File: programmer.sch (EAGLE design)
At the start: 2 parts, among them U1 ATMEGA328P_PDIP

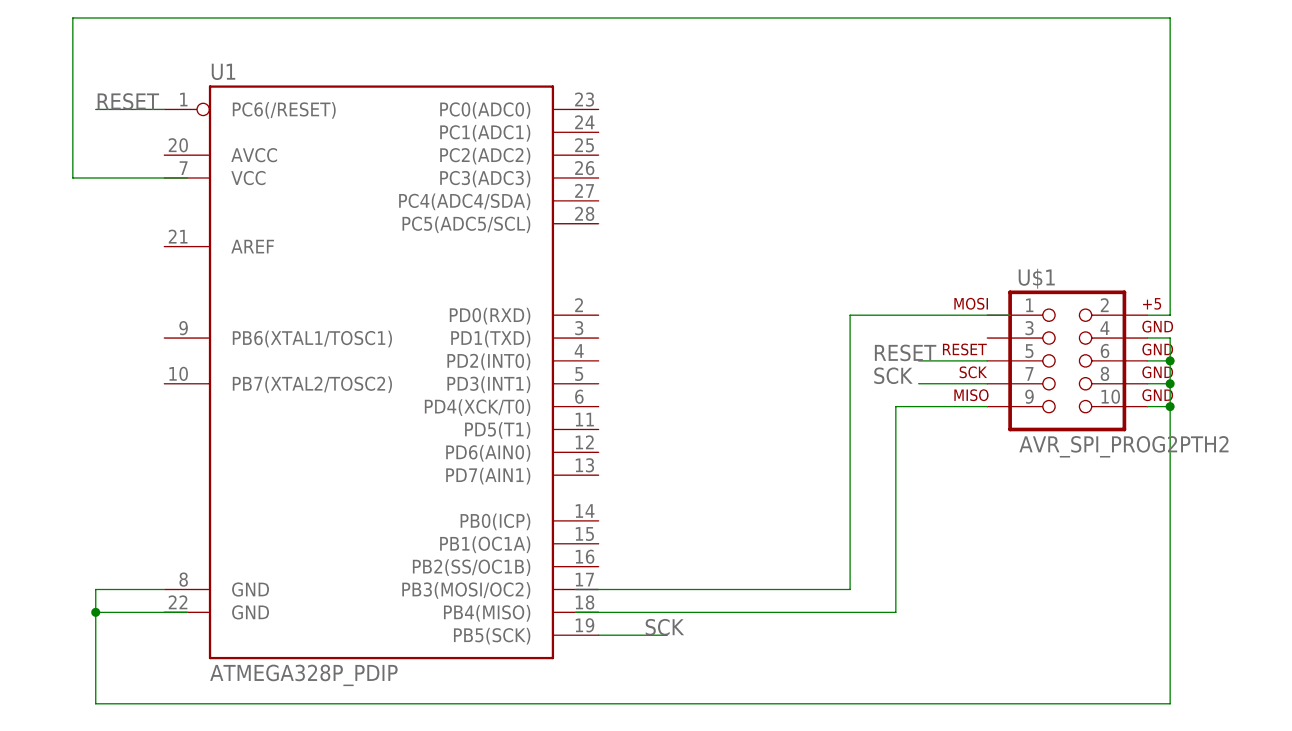
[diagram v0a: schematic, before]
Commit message: Added header for crystal and caps, cleaned VCC and GND lines
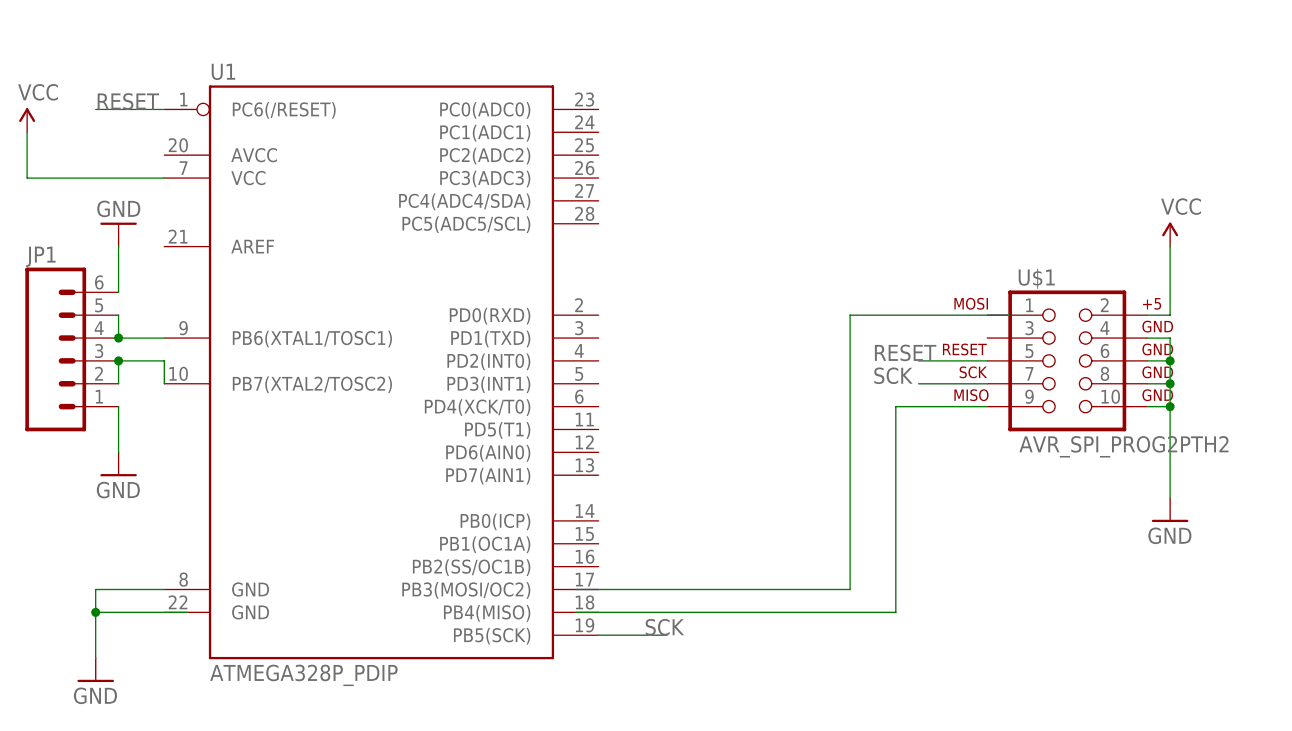
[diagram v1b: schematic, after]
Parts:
- added JP1: (no value), SparkFun-Connectors:M06LOCK
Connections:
- removed net N$4: U$1.10, U$1.4, U$1.6, U$1.8, U1.GND@1
- new net GND: JP1.1, JP1.6, U$1.10, U$1.4, U$1.6, U$1.8, U1.GND@1
- new net N$3: JP1.4, JP1.5, U1.PB6(XTAL1/TOSC1)
- new net N$5: JP1.2, JP1.3, U1.PB7(XTAL2/TOSC2)
- net VCC: now also U1.VCC
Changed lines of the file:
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@@
 <part name="U1" library="SparkFun-DigitalIC" deviceset="ATMEGA328P_PDIP" device=""/>
 <part name="U$1" library="SparkFun-Connectors" deviceset="AVR_SPI_PROG2" device="PTH2"/>
+<part name="JP1" library="SparkFun-Connectors" deviceset="M06" device="LOCK"/>
+<part name="GND1" library="SparkFun-Aesthetics" deviceset="GND" device=""/>
+<part name="GND2" library="SparkFun-Aesthetics" deviceset="GND" device=""/>
+<part name="GND3" library="SparkFun-Aesthetics" deviceset="GND" device=""/>
+<part name="GND4" library="SparkFun-Aesthetics" deviceset="GND" device=""/>
+<part name="SUPPLY1" library="SparkFun-Aesthetics" deviceset="VCC" device=""/>
+<part name="SUPPLY2" library="SparkFun-Aesthetics" deviceset="VCC" device=""/>
 </parts>
 <sheets>
@@
 <instance part="U1" gate="G$1" x="30.48" y="63.5"/>
 <instance part="U$1" gate="A" x="106.68" y="60.96"/>
+<instance part="JP1" gate="G$1" x="-2.54" y="60.96"/>
+<instance part="GND1" gate="1" x="119.38" y="43.18"/>
+<instance part="GND2" gate="1" x="0" y="25.4"/>
+<instance part="GND3" gate="1" x="2.54" y="48.26"/>
+<instance part="GND4" gate="1" x="2.54" y="76.2" rot="R180"/>
+<instance part="SUPPLY1" gate="G$1" x="119.38" y="73.66"/>
+<instance part="SUPPLY2" gate="G$1" x="-7.62" y="86.36"/>
 </instances>
 <busses>
@@
 </segment>
 </net>
-<net name="N$4" class="0">
+<net name="VCC" class="0">
 <segment>
+<pinref part="U$1" gate="A" pin="2"/>
+<wire x1="116.84" y1="66.04" x2="119.38" y2="66.04" width="0.1524" layer="91"/>
+<pinref part="SUPPLY1" gate="G$1" pin="VCC"/>
+<wire x1="119.38" y1="66.04" x2="119.38" y2="73.66" width="0.1524" layer="91"/>
+</segment>
+<segment>
+<pinref part="U1" gate="G$1" pin="VCC"/>
+<pinref part="SUPPLY2" gate="G$1" pin="VCC"/>
+<wire x1="7.62" y1="81.28" x2="-7.62" y2="81.28" width="0.1524" layer="91"/>
+<wire x1="-7.62" y1="81.28" x2="-7.62" y2="86.36" width="0.1524" layer="91"/>
+</segment>
+</net>
+<net name="N$3" class="0">
+<segment>
+<pinref part="U1" gate="G$1" pin="PB6(XTAL1/TOSC1)"/>
+<pinref part="JP1" gate="G$1" pin="4"/>
+<wire x1="7.62" y1="63.5" x2="2.54" y2="63.5" width="0.1524" layer="91"/>
+<pinref part="JP1" gate="G$1" pin="5"/>
+<wire x1="2.54" y1="63.5" x2="2.54" y2="66.04" width="0.1524" layer="91"/>
+<junction x="2.54" y="63.5"/>
+</segment>
+</net>
+<net name="N$5" class="0">
+<segment>
+<pinref part="JP1" gate="G$1" pin="3"/>
+<pinref part="U1" gate="G$1" pin="PB7(XTAL2/TOSC2)"/>
+<wire x1="2.54" y1="60.96" x2="7.62" y2="60.96" width="0.1524" layer="91"/>
+<wire x1="7.62" y1="60.96" x2="7.62" y2="58.42" width="0.1524" layer="91"/>
+<pinref part="JP1" gate="G$1" pin="2"/>
+<wire x1="2.54" y1="60.96" x2="2.54" y2="58.42" width="0.1524" layer="91"/>
+<junction x="2.54" y="60.96"/>
+</segment>
+</net>
+<net name="GND" class="0">
+<segment>
+<pinref part="U$1" gate="A" pin="8"/>
+<wire x1="116.84" y1="58.42" x2="119.38" y2="58.42" width="0.1524" layer="91"/>
+<pinref part="U$1" gate="A" pin="6"/>
+<wire x1="116.84" y1="60.96" x2="119.38" y2="60.96" width="0.1524" layer="91"/>
+<pinref part="U$1" gate="A" pin="4"/>
+<wire x1="116.84" y1="63.5" x2="119.38" y2="63.5" width="0.1524" layer="91"/>
+<wire x1="119.38" y1="63.5" x2="119.38" y2="60.96" width="0.1524" layer="91"/>
+<junction x="119.38" y="60.96"/>
+<wire x1="119.38" y1="60.96" x2="119.38" y2="58.42" width="0.1524" layer="91"/>
+<junction x="119.38" y="58.42"/>
+<wire x1="119.38" y1="58.42" x2="119.38" y2="55.88" width="0.1524" layer="91"/>
 <pinref part="U$1" gate="A" pin="10"/>
 <wire x1="116.84" y1="55.88" x2="119.38" y2="55.88" width="0.1524" layer="91"/>
-<wire x1="119.38" y1="55.88" x2="119.38" y2="22.86" width="0.1524" layer="91"/>
-<wire x1="119.38" y1="22.86" x2="0" y2="22.86" width="0.1524" layer="91"/>
-<wire x1="0" y1="22.86" x2="0" y2="33.02" width="0.1524" layer="91"/>
+<pinref part="GND1" gate="1" pin="GND"/>
+<wire x1="119.38" y1="55.88" x2="119.38" y2="45.72" width="0.1524" layer="91"/>
+<junction x="119.38" y="55.88"/>
+</segment>
+<segment>
 <wire x1="0" y1="33.02" x2="10.16" y2="33.02" width="0.1524" layer="91"/>
 <pinref part="U1" gate="G$1" pin="GND@1"/>
 <wire x1="7.62" y1="35.56" x2="0" y2="35.56" width="0.1524" layer="91"/>
 <wire x1="0" y1="35.56" x2="0" y2="33.02" width="0.1524" layer="91"/>
+<pinref part="GND2" gate="1" pin="GND"/>
+<wire x1="0" y1="33.02" x2="0" y2="27.94" width="0.1524" layer="91"/>
 <junction x="0" y="33.02"/>
-<pinref part="U$1" gate="A" pin="8"/>
-<wire x1="116.84" y1="58.42" x2="119.38" y2="58.42" width="0.1524" layer="91"/>
-<wire x1="119.38" y1="58.42" x2="119.38" y2="55.88" width="0.1524" layer="91"/>
-<junction x="119.38" y="55.88"/>
-<pinref part="U$1" gate="A" pin="6"/>
-<wire x1="116.84" y1="60.96" x2="119.38" y2="60.96" width="0.1524" layer="91"/>
-<wire x1="119.38" y1="60.96" x2="119.38" y2="58.42" width="0.1524" layer="91"/>
-<junction x="119.38" y="58.42"/>
-<pinref part="U$1" gate="A" pin="4"/>
-<wire x1="116.84" y1="63.5" x2="119.38" y2="63.5" width="0.1524" layer="91"/>
-<wire x1="119.38" y1="63.5" x2="119.38" y2="60.96" width="0.1524" layer="91"/>
-<junction x="119.38" y="60.96"/>
+</segment>
+<segment>
+<pinref part="JP1" gate="G$1" pin="1"/>
+<pinref part="GND3" gate="1" pin="GND"/>
+<wire x1="2.54" y1="55.88" x2="2.54" y2="50.8" width="0.1524" layer="91"/>
+</segment>
+<segment>
+<pinref part="JP1" gate="G$1" pin="6"/>
+<pinref part="GND4" gate="1" pin="GND"/>
+<wire x1="2.54" y1="68.58" x2="2.54" y2="73.66" width="0.1524" layer="91"/>
 </segment>
 </net>
-<net name="VCC" class="0">
-<segment>
-<pinref part="U$1" gate="A" pin="2"/>
-<wire x1="116.84" y1="66.04" x2="119.38" y2="66.04" width="0.1524" layer="91"/>
-<wire x1="119.38" y1="66.04" x2="119.38" y2="99.06" width="0.1524" layer="91"/>
-<wire x1="119.38" y1="99.06" x2="-2.54" y2="99.06" width="0.1524" layer="91"/>
-<wire x1="-2.54" y1="99.06" x2="-2.54" y2="81.28" width="0.1524" layer="91"/>
-<wire x1="-2.54" y1="81.28" x2="10.16" y2="81.28" width="0.1524" layer="91"/>
-</segment>
-</net>
